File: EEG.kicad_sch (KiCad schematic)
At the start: 0 parts

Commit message: top-level structure and ESP32-C6 pin assignments nearly sorted
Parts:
- added C21: 1u, Capacitor_SMD:C_1206_3216Metric, symbol Device:C
- added C7: 470p, Capacitor_SMD:C_0603_1608Metric, symbol Device:C
- added U11: MIC5205-3.3YM5, Package_TO_SOT_SMD:SOT-23-5, symbol Regulator_Linear:MIC5205-3.3YM5
- added U3: ADS1299, Package_QFP:TQFP-64_10x10mm_P0.5mm, symbol Analog_ADC:ADS1299
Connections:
- new net: C7.1, U11.4 (BP)
- new net AVDD: U11.5 (OUT), U3.19 (AVDD), U3.21 (AVDD), U3.22 (AVDD), U3.54 (AVDD1), U3.56 (AVDD), U3.59 (AVDD)
- new net CS: U3.39 (~{CS})
- new net DIN: U3.34 (DIN)
- new net DOUT: U3.43 (DOUT)
- new net EN: U11.3 (EN)
- new net GND: C21.2, C7.2, U11.2 (GND), U3.20 (AVSS), U3.23 (AVSS), U3.32 (AVSS), U3.33 (DGND), U3.49 (DGND), U3.51 (DGND), U3.53 (AVSS1), U3.57 (AVSS), U3.58 (AVSS)
- new net SCLK: U3.40 (SCLK)
- new net VDD: C21.1, U11.1 (IN), U3.48 (DVDD), U3.50 (DVDD)
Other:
- note added: "EN HIGH = Enable (active)"
- company: (none) -> Sunrise designs
- title: (none) -> Open polysomnography board

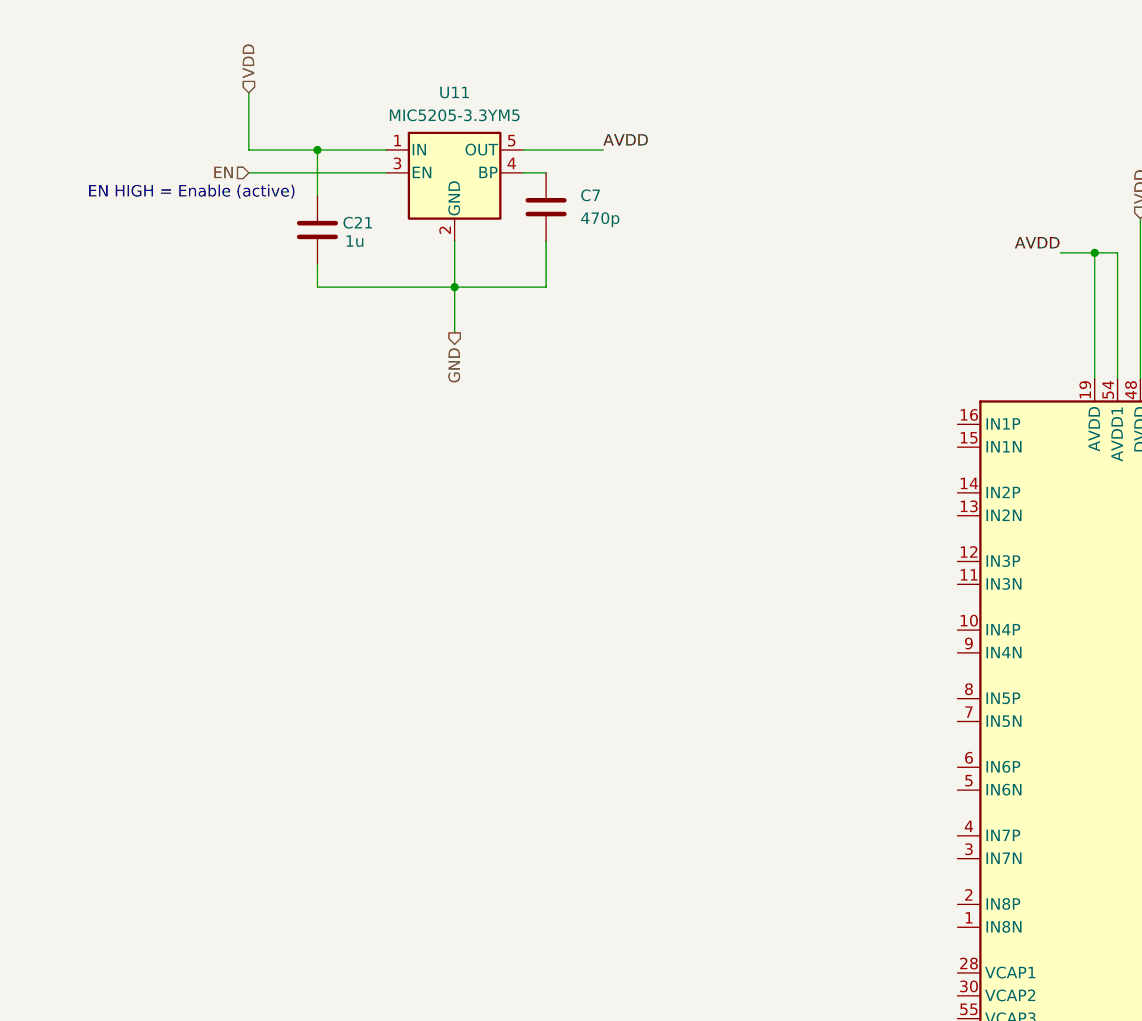
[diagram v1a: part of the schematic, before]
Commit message: text comments sections added
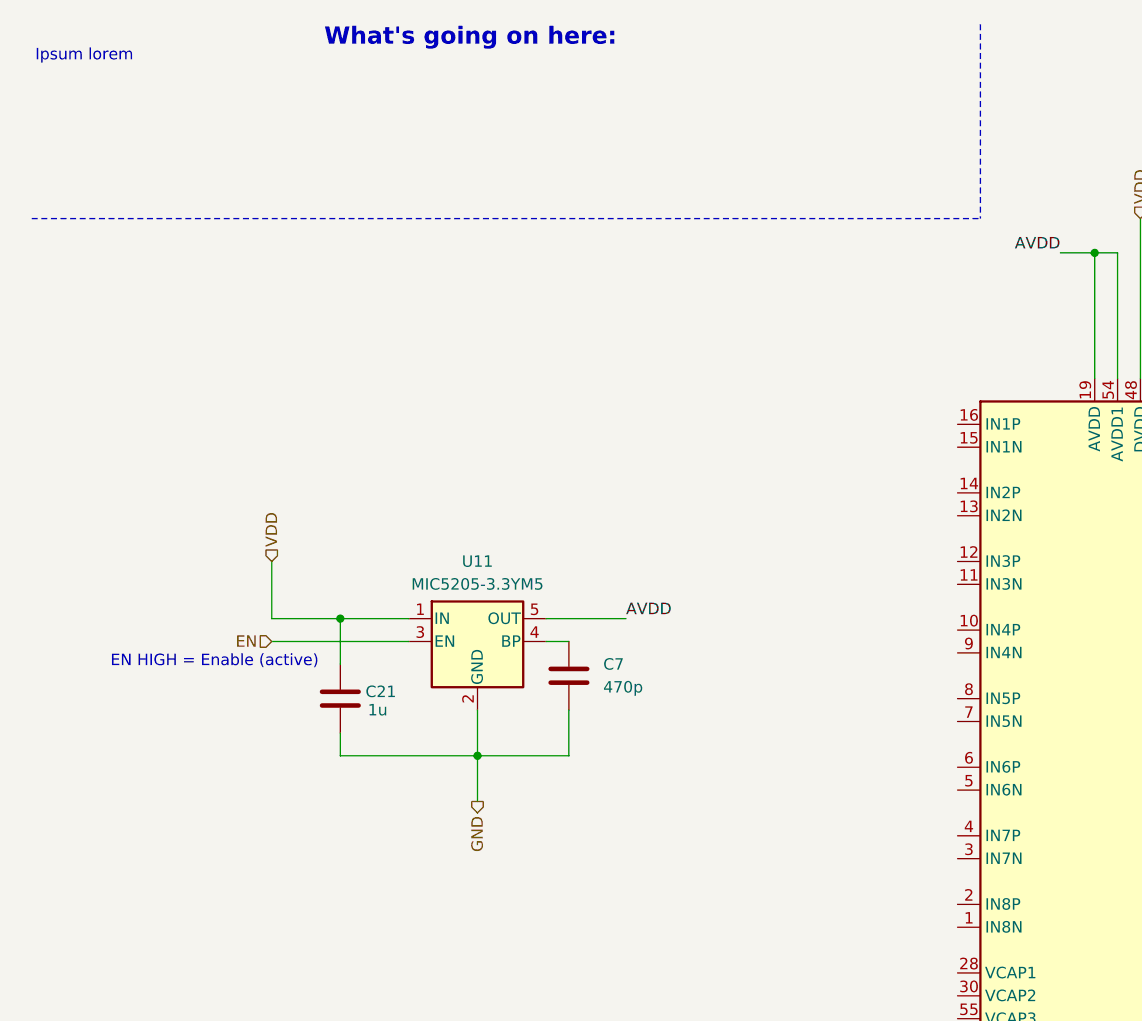
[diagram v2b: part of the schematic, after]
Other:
- note added: "Ipsum lorem"
- note added: "What's going on here:"
- moved on the sheet: C21, C7, U11
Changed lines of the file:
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@@
 		(company "Sunrise designs")
+	)
+	(text "Ipsum lorem\n"
+		(exclude_from_sim no)
+		(at 18.542 16.256 0)
+		(effects
+			(font
+				(size 1.27 1.27)
+				(color 132 0 0 1)
+			)
+		)
 	)
 	(text "EN HIGH = Enable (active)\n"
 		(exclude_from_sim no)
-		(at 30.48 31.496 0)
-		(effects
-			(font
-				(size 1.27 1.27)
+		(at 33.02 83.566 0)
+		(effects
+			(font
+				(size 1.27 1.27)
+			)
+		)
+	)
+	(text "What's going on here:\n"
+		(exclude_from_sim no)
+		(at 61.468 14.224 0)
+		(effects
+			(font
+				(size 1.905 1.905)
+				(thickness 0.381)
+				(bold yes)
+				(color 132 0 0 1)
 			)
 		)
 	)
 	(junction
-		(at 44.45 26.67)
+		(at 46.99 78.74)
 		(diameter 0)
 		(color 0 0 0 0)
@@
 	)
 	(junction
-		(at 59.69 41.91)
+		(at 62.23 93.98)
 		(diameter 0)
 		(color 0 0 0 0)
@@
 	(wire
 		(pts
-			(xy 59.69 36.83) (xy 59.69 41.91)
+			(xy 62.23 88.9) (xy 62.23 93.98)
 		)
 		(stroke
@@
 	(wire
 		(pts
-			(xy 59.69 41.91) (xy 59.69 46.99)
-		)
-		(stroke
-			(width 0)
-			(type default)
-		)
-	)
-	(wire
-		(pts
-			(xy 44.45 39.37) (xy 44.45 41.91)
-		)
-		(stroke
-			(width 0)
-			(type default)
-		)
-	)
-	(wire
-		(pts
-			(xy 36.83 29.21) (xy 52.07 29.21)
+			(xy 62.23 93.98) (xy 62.23 99.06)
+		)
+		(stroke
+			(width 0)
+			(type default)
+		)
+	)
+	(wire
+		(pts
+			(xy 46.99 91.44) (xy 46.99 93.98)
+		)
+		(stroke
+			(width 0)
+			(type default)
+		)
+	)
+	(wire
+		(pts
+			(xy 39.37 81.28) (xy 54.61 81.28)
 		)
 		(stroke
@@
 	(wire
 		(pts
-			(xy 44.45 41.91) (xy 59.69 41.91)
+			(xy 46.99 93.98) (xy 62.23 93.98)
 		)
 		(stroke
@@
 	(wire
 		(pts
-			(xy 59.69 41.91) (xy 69.85 41.91)
+			(xy 62.23 93.98) (xy 72.39 93.98)
 		)
 		(stroke
@@
 	(wire
 		(pts
-			(xy 67.31 29.21) (xy 69.85 29.21)
+			(xy 69.85 81.28) (xy 72.39 81.28)
 		)
 		(stroke
@@
 	(wire
 		(pts
-			(xy 69.85 36.83) (xy 69.85 41.91)
-		)
-		(stroke
-			(width 0)
-			(type default)
-		)
-	)
-	(wire
-		(pts
-			(xy 44.45 26.67) (xy 44.45 31.75)
+			(xy 72.39 88.9) (xy 72.39 93.98)
+		)
+		(stroke
+			(width 0)
+			(type default)
+		)
+	)
+	(wire
+		(pts
+			(xy 46.99 78.74) (xy 46.99 83.82)
 		)
 		(stroke
@@
 	(wire
 		(pts
-			(xy 36.83 20.32) (xy 36.83 26.67)
+			(xy 39.37 72.39) (xy 39.37 78.74)
 		)
 		(stroke
@@
 	(wire
 		(pts
-			(xy 67.31 26.67) (xy 76.2 26.67)
+			(xy 69.85 78.74) (xy 78.74 78.74)
 		)
 		(stroke
@@
 	(wire
 		(pts
-			(xy 52.07 26.67) (xy 44.45 26.67)
-		)
-		(stroke
-			(width 0)
-			(type default)
-		)
-	)
-	(wire
-		(pts
-			(xy 44.45 26.67) (xy 36.83 26.67)
+			(xy 54.61 78.74) (xy 46.99 78.74)
+		)
+		(stroke
+			(width 0)
+			(type default)
+		)
+	)
+	(polyline
+		(pts
+			(xy 12.7 34.29) (xy 118.11 34.29)
+		)
+		(stroke
+			(width 0)
+			(type dash)
+			(color 132 0 0 1)
+		)
+	)
+	(polyline
+		(pts
+			(xy 118.11 12.7) (xy 118.11 34.29)
+		)
+		(stroke
+			(width 0)
+			(type dash)
+			(color 132 0 0 1)
+		)
+	)
+	(wire
+		(pts
+			(xy 46.99 78.74) (xy 39.37 78.74)
 		)
 		(stroke
@@
 	)
 	(label "AVDD"
-		(at 76.2 26.67 0)
+		(at 78.74 78.74 0)
 		(effects
 			(font
@@
 	(hierarchical_label "GND"
 		(shape output)
-		(at 59.69 46.99 270)
+		(at 62.23 99.06 270)
 		(effects
 			(font
@@
 	(hierarchical_label "VDD"
 		(shape input)
-		(at 36.83 20.32 90)
+		(at 39.37 72.39 90)
 		(effects
 			(font
@@
 	(hierarchical_label "EN"
 		(shape input)
-		(at 36.83 29.21 180)
+		(at 39.37 81.28 180)
 		(effects
 			(font
@@
 	(symbol
 		(lib_id "Device:C")
-		(at 69.85 33.02 0)
+		(at 72.39 85.09 0)
 		(unit 1)
 		(body_style 1)
@@
 		(fields_autoplaced yes)
 		(property "Reference" "C7"
-			(at 73.66 31.7499 0)
+			(at 76.2 83.8199 0)
 			(show_name no)
 			(do_not_autoplace no)
@@
 		)
 		(property "Value" "470p"
-			(at 73.66 34.2899 0)
+			(at 76.2 86.3599 0)
 			(show_name no)
 			(do_not_autoplace no)
@@
 		)
 		(property "Footprint" "Capacitor_SMD:C_0603_1608Metric"
-			(at 70.8152 36.83 0)
+			(at 73.3552 88.9 0)
 			(hide yes)
 			(show_name no)
@@
 		)
 		(property "Datasheet" ""
-			(at 69.85 33.02 0)
+			(at 72.39 85.09 0)
 			(hide yes)
 			(show_name no)
@@
 		)
 		(property "Description" "Unpolarized capacitor"
-			(at 69.85 33.02 0)
+			(at 72.39 85.09 0)
 			(hide yes)
 			(show_name no)
@@
 	(symbol
 		(lib_id "Regulator_Linear:MIC5205-3.3YM5")
-		(at 59.69 29.21 0)
+		(at 62.23 81.28 0)
 		(unit 1)
 		(body_style 1)
@@
 		(fields_autoplaced yes)
 		(property "Reference" "U11"
-			(at 59.69 20.32 0)
+			(at 62.23 72.39 0)
 			(show_name no)
 			(do_not_autoplace no)
@@
 		)
 		(property "Value" "MIC5205-3.3YM5"
-			(at 59.69 22.86 0)
+			(at 62.23 74.93 0)
 			(show_name no)
 			(do_not_autoplace no)
@@
 		)
 		(property "Footprint" "Package_TO_SOT_SMD:SOT-23-5"
-			(at 59.69 20.955 0)
+			(at 62.23 73.025 0)
 			(hide yes)
 			(show_name no)
@@
 		)
 		(property "Datasheet" "http://ww1.microchip.com/downloads/en/DeviceDoc/20005785A.pdf"
-			(at 59.69 29.21 0)
+			(at 62.23 81.28 0)
 			(hide yes)
 			(show_name no)
@@
 		)
 		(property "Description" "150mA low dropout linear regulator, fixed 3.3V output, SOT-23-5"
-			(at 59.69 29.21 0)
+			(at 62.23 81.28 0)
 			(hide yes)
 			(show_name no)
@@
 	(symbol
 		(lib_id "Device:C")
-		(at 44.45 35.56 0)
+		(at 46.99 87.63 0)
 		(unit 1)
 		(body_style 1)
@@
 		(dnp no)
 		(property "Reference" "C21"
-			(at 47.244 34.798 0)
+			(at 49.784 86.868 0)
 			(show_name no)
 			(do_not_autoplace no)
@@
 		)
 		(property "Value" "1u"
-			(at 47.498 36.83 0)
+			(at 50.038 88.9 0)
 			(show_name no)
 			(do_not_autoplace no)
@@
 		)
 		(property "Footprint" "Capacitor_SMD:C_1206_3216Metric"
-			(at 45.4152 39.37 0)
+			(at 47.9552 91.44 0)
 			(hide yes)
 			(show_name no)
@@
 		)
 		(property "Datasheet" ""
-			(at 44.45 35.56 0)
+			(at 46.99 87.63 0)
 			(hide yes)
 			(show_name no)
@@
 		)
 		(property "Description" "Unpolarized capacitor"
-			(at 44.45 35.56 0)
-			(hide yes)
-			(show_name no)
+			(at 46.99 87.63 0)
+			(hide yes)
+			(show_name no)

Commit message: some work on sch and docs added
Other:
- note added: "DIN 42 802 (often cited as DIN 42802-1 or -2) defines the standard for 1.5mm "touch-proof" safety connectors used in medical, biomedical, EEG, and EMG recording systems"
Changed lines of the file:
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@@
+		)
+	)
+	(text "DIN 42 802 (often cited as DIN 42802-1 or -2) defines the standard for 1.5mm \"touch-proof\" safety connectors used in medical, biomedical, EEG, and EMG recording systems"
+		(exclude_from_sim no)
+		(at 109.474 160.528 0)
+		(effects
+			(font
+				(size 1.27 1.27)
+			)
 		)
 	)
